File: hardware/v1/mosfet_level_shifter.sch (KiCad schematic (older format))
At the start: 3 parts, among them Q1 2N7000

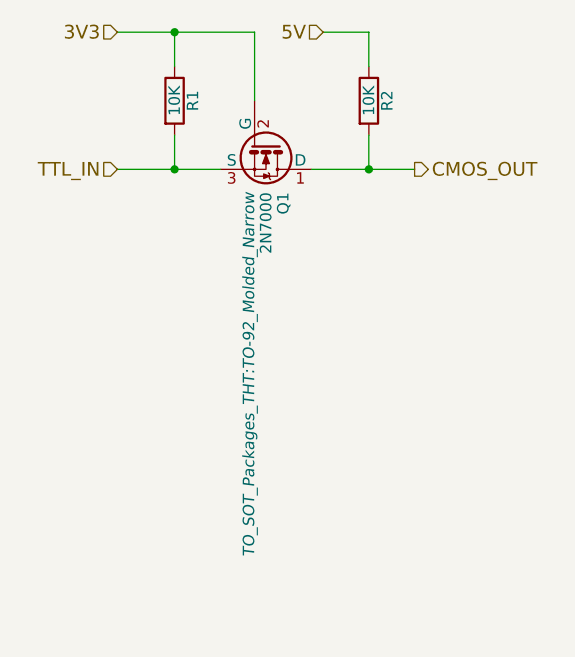
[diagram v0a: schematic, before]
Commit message: Add keys-8 schematic and initial pcb layout file.
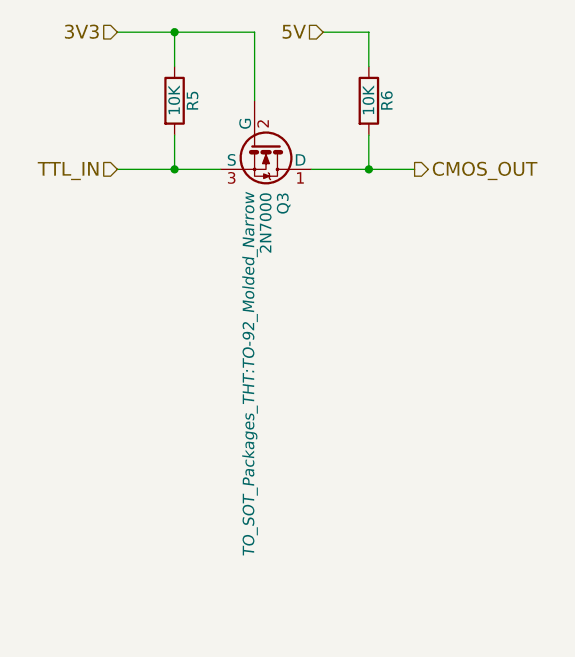
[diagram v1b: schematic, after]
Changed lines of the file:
@@
 $Descr A4 11693 8268
 encoding utf-8
-Sheet 7 25
+Sheet 7 26
 Title ""
 Date ""
@@
 AR Path="/57A2FF40/57A33FC0/5798C5FD" Ref="R3"  Part="1"
 AR Path="/57A2FF40/57A33FD2/5798C5FD" Ref="R5"  Part="1"
-F 0 "R1" V 1230 1000 50  0000 C CNN
+F 0 "R5" V 1230 1000 50  0000 C CNN
 F 1 "10K" V 1150 1000 50  0000 C CNN
 F 2 "Resistors_ThroughHole:Resistor_Horizontal_RM10mm" V 1080 1000 50  0001 C CNN
@@
 AR Path="/57A2FF40/57A33FC0/5798C628" Ref="R4"  Part="1"
 AR Path="/57A2FF40/57A33FD2/5798C628" Ref="R6"  Part="1"
-F 0 "R2" V 2080 1000 50  0000 C CNN
+F 0 "R6" V 2080 1000 50  0000 C CNN
 F 1 "10K" V 2000 1000 50  0000 C CNN
 F 2 "Resistors_ThroughHole:Resistor_Horizontal_RM10mm" V 1930 1000 50  0001 C CNN
@@
 AR Path="/57A2FF40/57A33FC0/5798C66E" Ref="Q2"  Part="1"
 AR Path="/57A2FF40/57A33FD2/5798C66E" Ref="Q3"  Part="1"
-F 0 "Q1" H 1750 1275 50  0000 L CNN
+F 0 "Q3" H 1750 1275 50  0000 L CNN
 F 1 "2N7000" H 1750 1200 50  0000 L CNN
 F 2 "TO_SOT_Packages_THT:TO-92_Molded_Narrow" H 1750 1125 50  0000 L CIN
